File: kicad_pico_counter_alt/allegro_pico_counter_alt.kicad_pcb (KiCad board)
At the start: 2 copper layers, 50.8 x 53.3 mm, 36 parts, among them J1 power, J10 Conn_01x01, J11 Conn_01x01, J12 Conn_01x01, J13 Conn_01x01, J14 Conn_01x01, J15 jump, J16 jump, J2 i2c, J3 display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

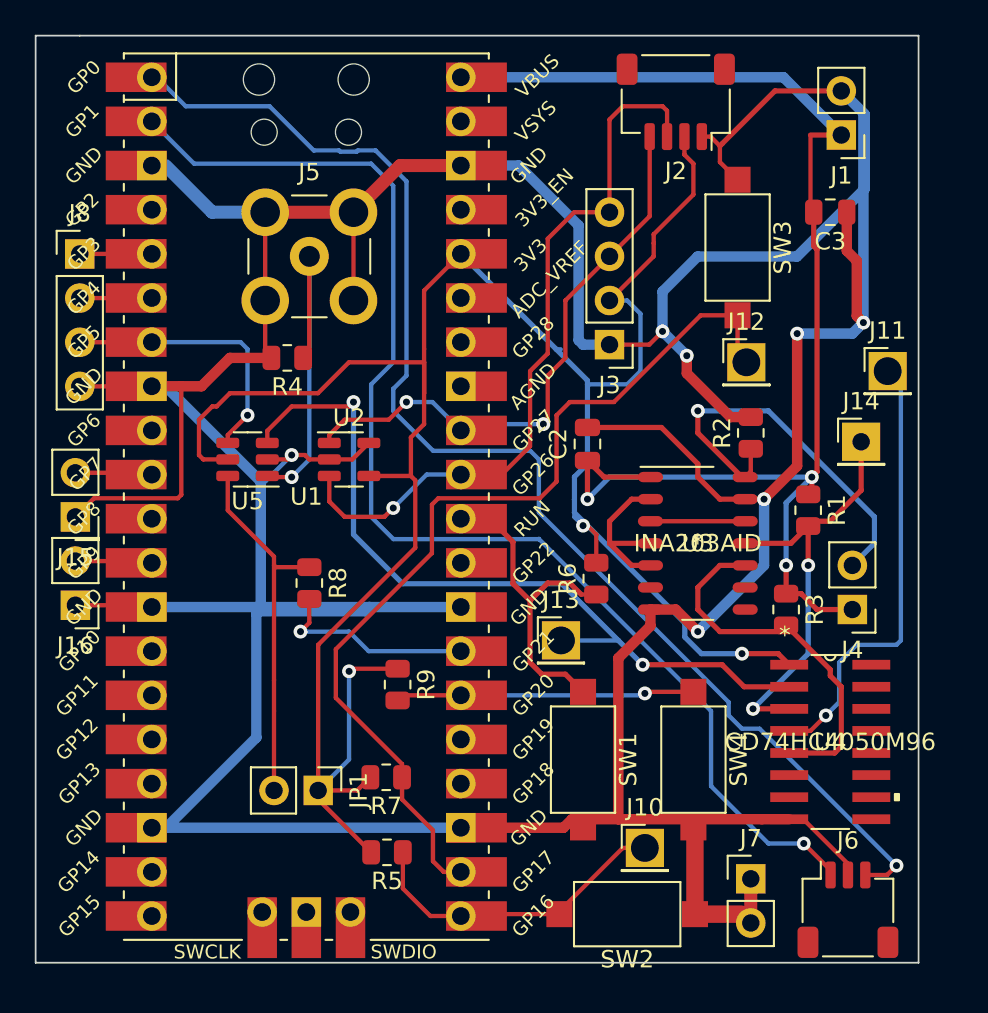
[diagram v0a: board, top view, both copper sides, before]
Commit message: add new pcb and schematic version, and change a pin in the code
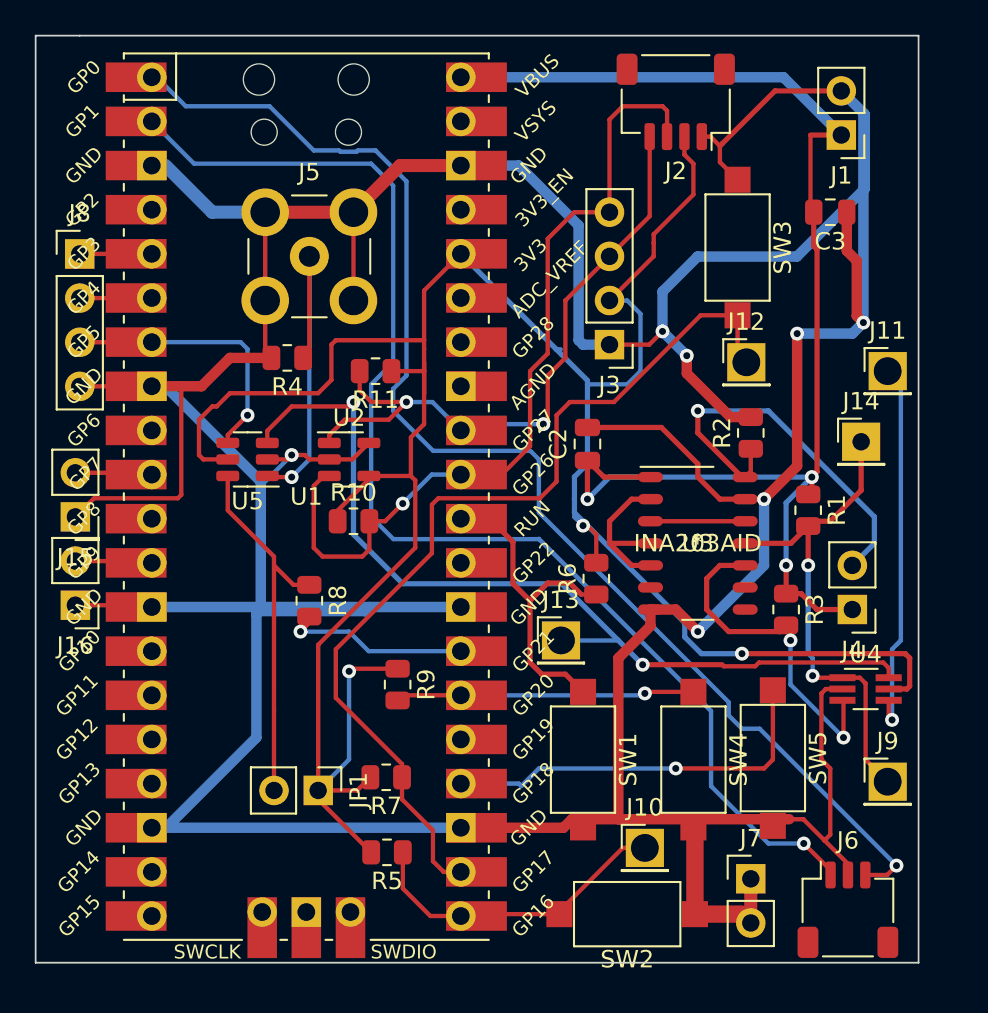
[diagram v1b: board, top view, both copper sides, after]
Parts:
- added J9: Conn_01x01, Connector_PinHeader_2.54mm:PinHeader_1x01_P2.54mm_Vertical, F.Cu at (167.1, 117.9)
- added R10: R, Resistor_SMD:R_0805_2012Metric, F.Cu at (136.4, 102.9)
- added R11: R, Resistor_SMD:R_0805_2012Metric, F.Cu at (137.7, 94.2)
- added SW5: SW_Push, Button_Switch_SMD:SW_SPST_CK_RS282G05A3, F.Cu at (160.5, 116.5)
- U4: value CD74HC4050M96 -> 74HC2G34GW; footprint CD74HC4050M96:CD74HC4050M96 -> Package_TO_SOT_SMD:SOT-363_SC-70-6_Handsoldering
- moved U4 3.66 mm to (165.9, 112.5)
- moved R8 1.02 mm to (133.9, 107.4)
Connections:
- R1 pad 2: Net-(J14-Pin_1) -> Net-(J9-Pin_1)
- U1 pad 24: unconnected-(U1-GPIO18-Pad24) -> Net-(U1-GPIO18)
- U3 pad 11: Net-(J14-Pin_1) -> Net-(J9-Pin_1)
- U4 pad 1: +3.3V -> Net-(J9-Pin_1)
- U4 pad 2: Net-(J13-Pin_1) -> GND
- U4 pad 3: Net-(J14-Pin_1) -> Net-(U3-CMP2_OUT)
- U4 pad 5: Net-(U3-CMP2_OUT) -> +3.3V
- U4 pad 6: unconnected-(U4-3Y-Pad6) -> Net-(J13-Pin_1)
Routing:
- net Net-(J9-Pin_1): track 0.00 -> 28.9 mm, vias 0 -> 2
- net Net-(J14-Pin_1): track 24.6 -> 0.00 mm, vias 2 -> 0
- net Net-(U1-GPIO18): track 0.00 -> 22.6 mm, vias 0 -> 1
- net +3.3V: track 135.0 -> 151.6 mm
- net GND: track 315.3 -> 325.4 mm
- net Net-(J13-Pin_1): track 46.0 -> 52.0 mm
- net Net-(J2-Pin_3): track 42.2 -> 48.0 mm
- net Net-(J2-Pin_4): track 35.2 -> 39.2 mm
- net Net-(J11-Pin_1): track 25.7 -> 22.2 mm
- net Net-(U3-CMP2_OUT): track 21.7 -> 19.5 mm, vias 0 -> 2
- net Net-(U1-GPIO21): track 11.8 -> 10.4 mm
